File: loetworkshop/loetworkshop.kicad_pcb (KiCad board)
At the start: 2 copper layers, 50 x 100 mm, 14 parts, among them SW1 ON, SW2 OFF, SW3 SW_Push_SPDT, U1 CD40107BE, U2 NE555P

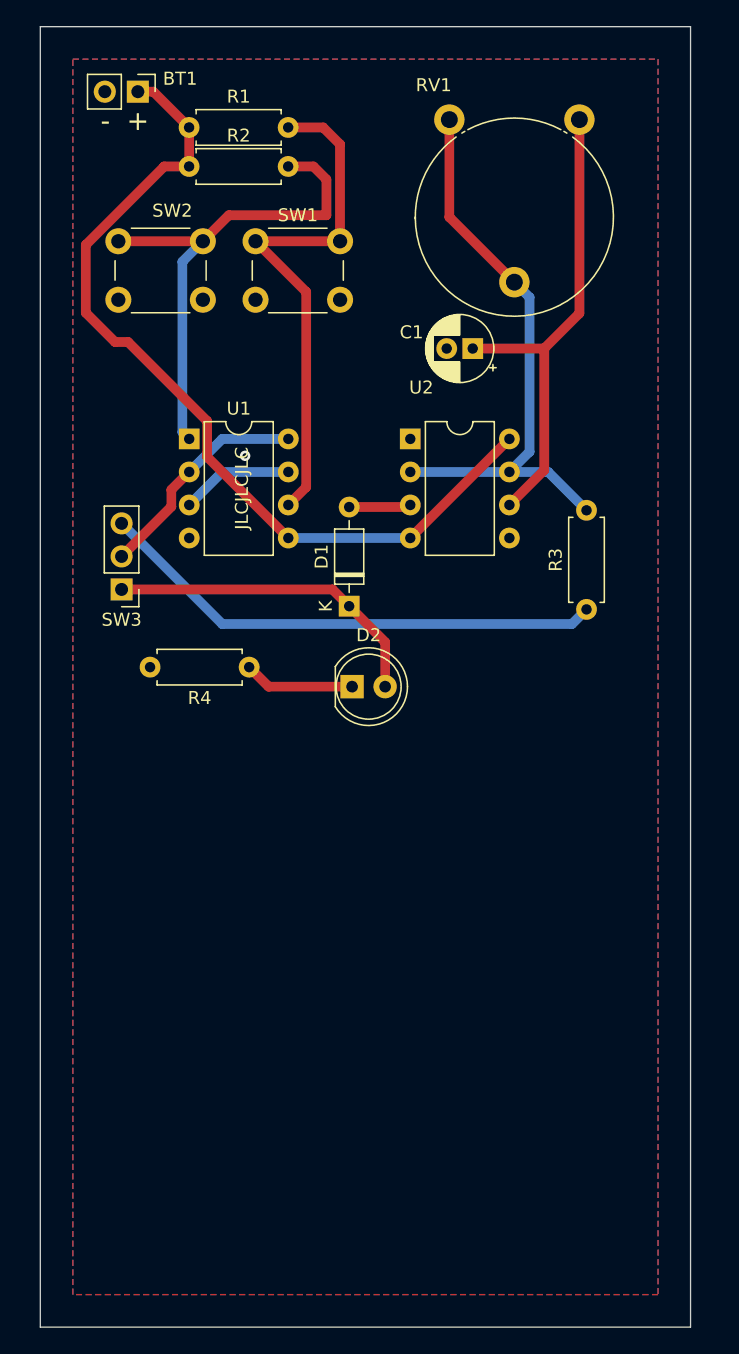
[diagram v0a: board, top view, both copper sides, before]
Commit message: added third soldering challenge
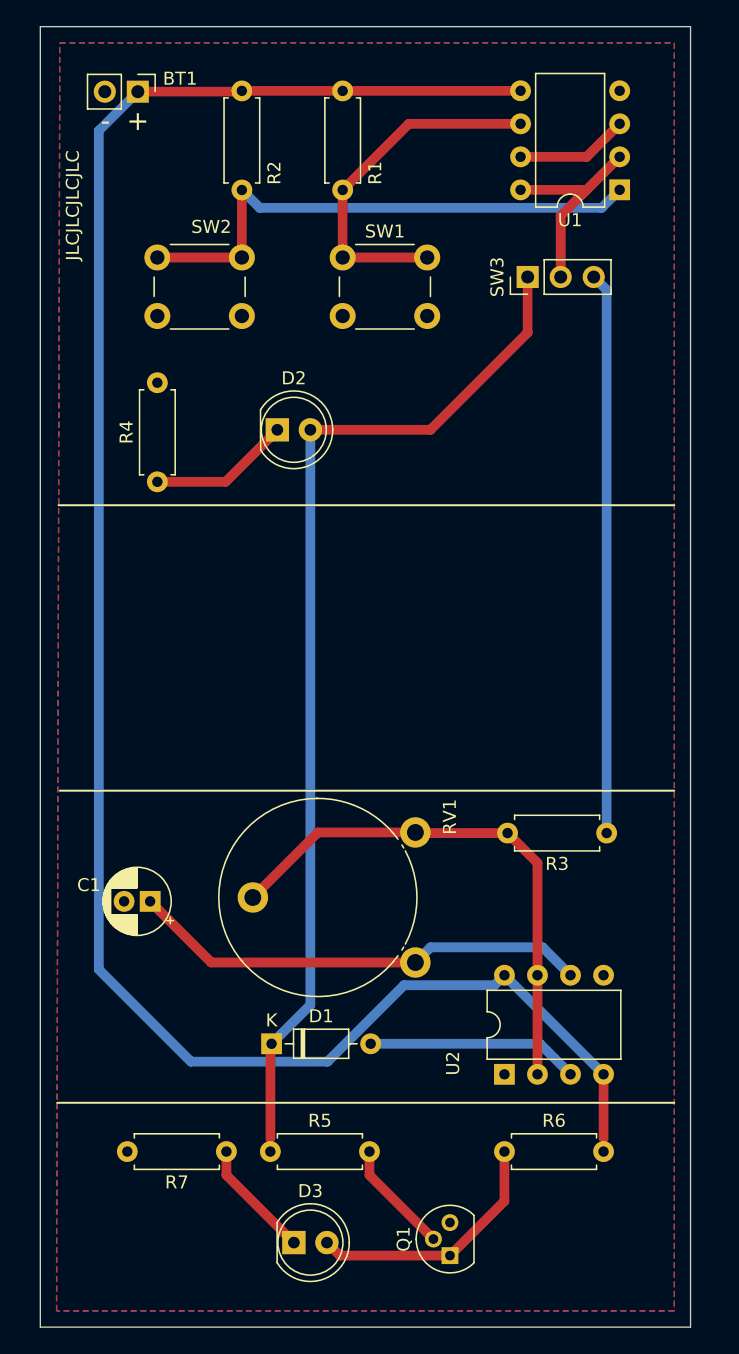
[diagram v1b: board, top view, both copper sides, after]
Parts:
- added D3: LED, LED_THT:LED_D5.0mm, F.Cu at (32.0, 106.0)
- added Q1: Q_NPN_CBE, Package_TO_SOT_THT:TO-92, F.Cu at (44.0, 107.0)
- added R5: 1K, Resistor_THT:R_Axial_DIN0207_L6.3mm_D2.5mm_P7.62mm_Horizontal, F.Cu at (30.2, 99.0)
- added R6: 1K, Resistor_THT:R_Axial_DIN0207_L6.3mm_D2.5mm_P7.62mm_Horizontal, F.Cu at (48.2, 99.0)
- added R7: 1K, Resistor_THT:R_Axial_DIN0207_L6.3mm_D2.5mm_P7.62mm_Horizontal, F.Cu at (26.8, 99.0)
- moved RV1 54.9 mm to (41.3, 74.5), turned to 180 degrees
- moved U2 49.4 mm to (48.2, 93.1), turned to 90 degrees
- moved C1 49.2 mm to (20.9, 79.8)
- moved SW3 39.4 mm to (50.0, 31.8), turned to 90 degrees
- moved U1 38.2 mm to (57.0, 25.1), turned to 180 degrees
- moved D1 34.2 mm to (30.3, 90.7), turned to 0 degrees
- moved D2 20.6 mm to (30.7, 43.5)
- moved R3 17.3 mm to (56.0, 74.5), turned to 180 degrees
- moved R4 15.9 mm to (21.5, 47.5), turned to 90 degrees
- moved R1 12.1 mm to (35.8, 17.4), turned to -90 degrees
- moved R2 7.09 mm to (28.0, 17.4), turned to -90 degrees
- moved SW1 6.82 mm to (35.8, 30.2)
- moved SW2 3.25 mm to (21.5, 30.2)
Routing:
- net +9V: track 68.3 -> 150.8 mm
- net /Drive_Constant: track 25.4 -> 79.9 mm
- net Net-(D3-Pad2): track 0.00 -> 19.6 mm
- net /On_Button: track 40.9 -> 27.5 mm
- net Net-(D1-Pad2): track 4.77 -> 16.3 mm
- net Net-(D3-Pad1): track 0.00 -> 9.15 mm
- net Net-(Q1-Pad2): track 0.00 -> 8.77 mm
- net /Discharge: track 45.1 -> 41.2 mm
- net /Drive_Timer: track 39.4 -> 43.2 mm
- net /Off_Button: track 39.0 -> 41.9 mm
- net Net-(D2-Pad1): track 8.54 -> 10.9 mm
- net /Threshold: track 37.4 -> 35.6 mm
- net Net-(SW3-Pad2): track 17.3 -> 16.2 mm
- net GND: vias 1 -> 0
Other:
- board text added: "JLCJLCJLCJLC"
- board text removed: "JLCJLCJLC"

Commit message: new pcb layout
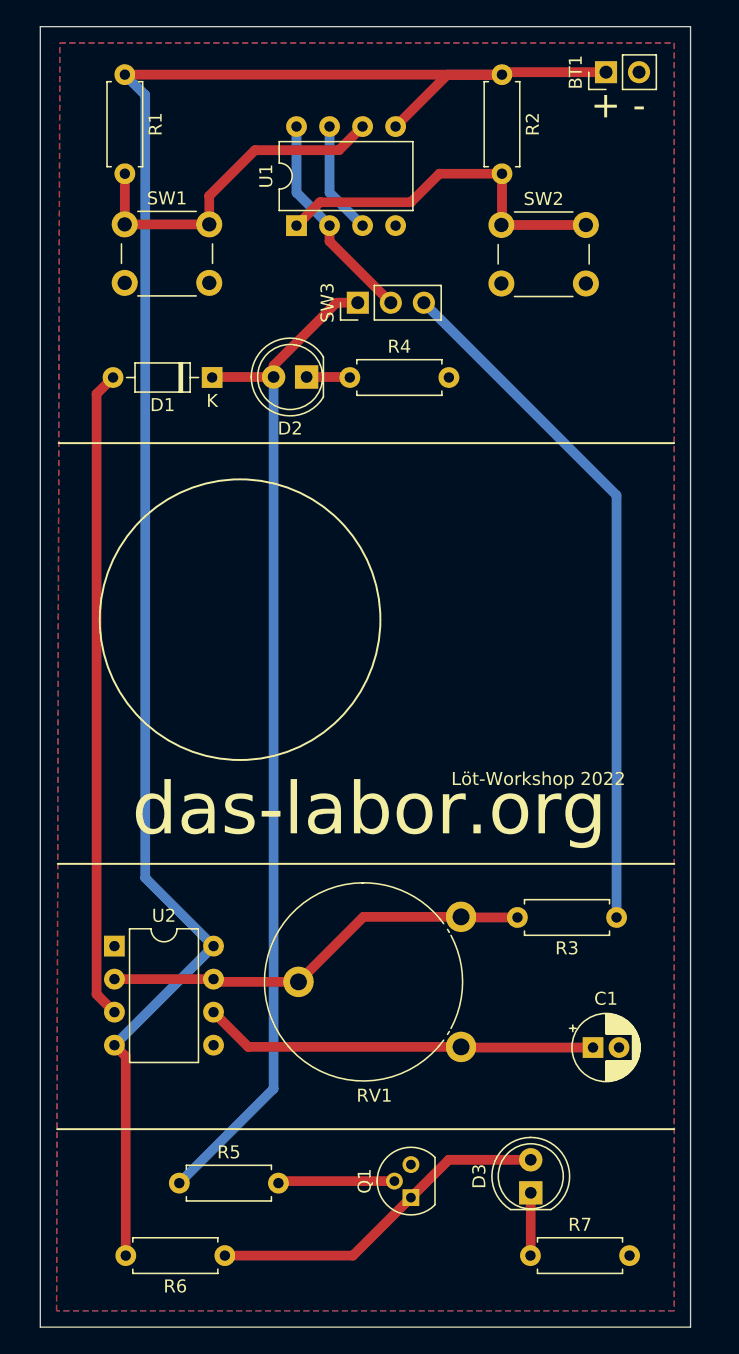
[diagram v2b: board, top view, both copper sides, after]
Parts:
- R1, R2: value 50K -> 10K
- R5: value 1K -> 10K
- moved D1 51.4 mm to (25.7, 39.5), turned to 180 degrees
- moved BT1 36.0 mm to (56.0, 16.0), turned to 90 degrees
- moved C1 35.9 mm to (55.0, 91.0), turned to 0 degrees
- moved U2 31.6 mm to (18.2, 83.2), turned to 0 degrees
- moved SW2 26.6 mm to (48.0, 27.8)
- moved U1 25.0 mm to (32.2, 27.8), turned to 90 degrees
- moved R7 24.7 mm to (50.2, 107.0), turned to 0 degrees
- moved R6 22.9 mm to (26.7, 107.0), turned to 180 degrees
- moved R2 20.0 mm to (48.0, 16.2)
- moved D3 18.6 mm to (50.2, 102.2), turned to 90 degrees
- moved SW1 17.0 mm to (19.0, 27.7)
- moved R4 16.8 mm to (36.3, 39.5), turned to 0 degrees
- moved R1 16.8 mm to (19.0, 16.2)
- moved SW3 13.2 mm to (36.9, 33.7)
- moved R5 7.41 mm to (23.2, 101.4)
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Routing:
- net Net-(D1-Pad2): track 16.3 -> 49.9 mm
- net /Off_Button: track 41.9 -> 28.1 mm
- net /Drive_Timer: track 43.2 -> 53.4 mm
- net /Discharge: track 41.2 -> 33.2 mm
- net Net-(D2-Pad1): track 10.9 -> 3.34 mm
- net Net-(D3-Pad2): track 19.6 -> 26.6 mm
- net +9V: track 150.8 -> 144.1 mm
- net /Threshold: track 35.6 -> 30.3 mm
- net Net-(D3-Pad1): track 9.15 -> 4.84 mm
- net /On_Button: track 27.5 -> 26.6 mm
- net /Drive_Constant: track 79.9 -> 79.1 mm
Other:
- board text added: "Created by: CodingChris - Kanga - Favo"
- board text added: "Löt-Workshop 2022"
- board text added: "das-labor.org"

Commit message: rev 1
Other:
- board text added: "Created by: CodingChris - Favo - Kanga"
- board text added: "Schnupperlöten"
- board text removed: "Created by: CodingChris - Kanga - Favo"
- board text removed: "Löt-Workshop 2022"
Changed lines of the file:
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@@
   (gr_line (start 12.5 12.5) (end 62.5 12.5) (layer "Edge.Cuts") (width 0.1))
   (gr_line (start 12.5 112.5) (end 12.5 12.5) (layer "Edge.Cuts") (width 0.1))
-  (gr_text "Created by:\nCodingChris - Kanga - Favo" (at 46.975 74.6) (layer "B.SilkS")
+  (gr_text "Created by:\nCodingChris - Favo - Kanga" (at 47.375 73.475) (layer "B.SilkS")
     (effects (font (size 1 1) (thickness 0.15)) (justify mirror))
   )
@@
     (effects (font (size 2 2) (thickness 0.3)))
   )
-  (gr_text "Löt-Workshop 2022" (at 50.8 70.35) (layer "F.SilkS")
+  (gr_text "Schnupperlöten\n" (at 52.8 70.375) (layer "F.SilkS")
     (effects (font (size 1 1) (thickness 0.15)))
   )

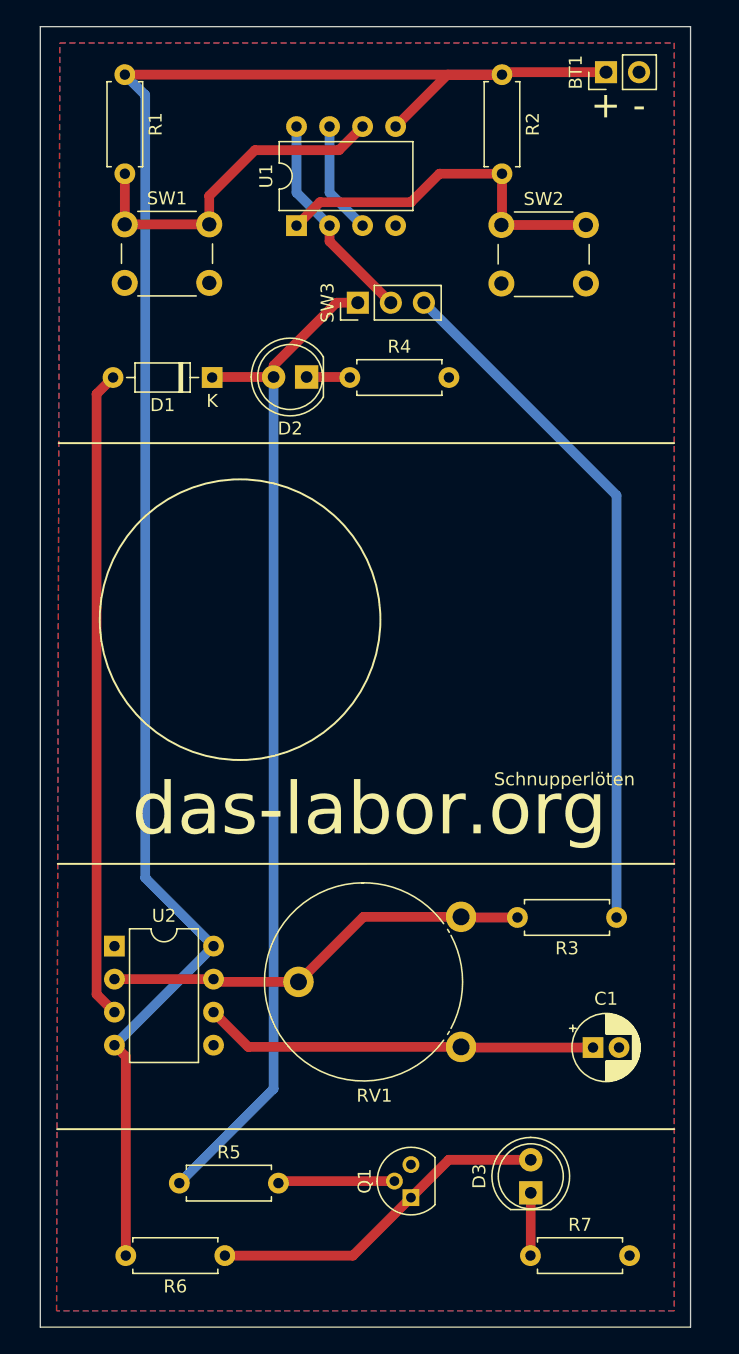
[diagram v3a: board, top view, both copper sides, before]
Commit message: rev 1.1 - fixed IC Pinout in the Footprint
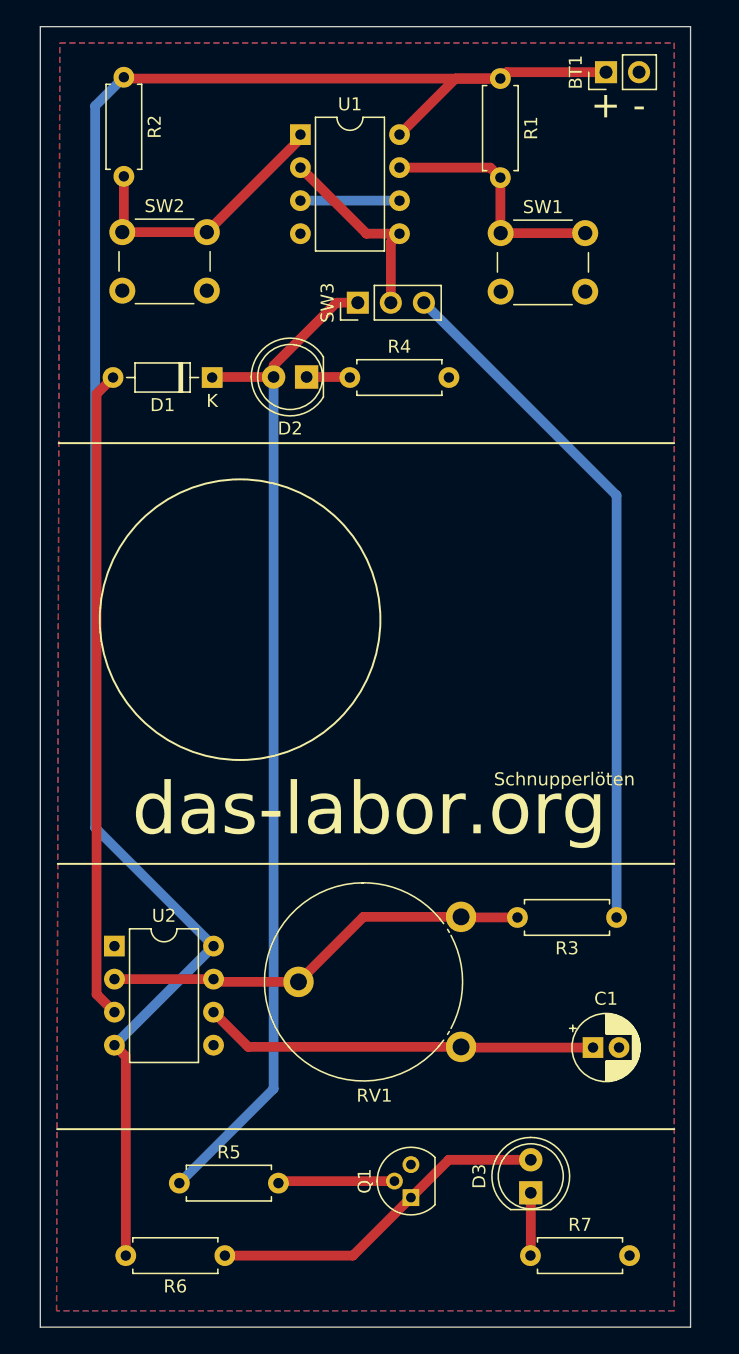
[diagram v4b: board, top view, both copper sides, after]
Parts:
- U1: footprint Package_DIP:DIP-8_W7.62mm -> switch_footprints:DIP-8_W7.62mm_InvertedDualRow
- moved SW2 29.2 mm to (18.8, 28.3)
- moved R2 29.1 mm to (18.9, 16.4)
- moved SW1 28.9 mm to (47.9, 28.4)
- moved R1 28.9 mm to (47.9, 16.5)
- moved U1 7.01 mm to (32.5, 20.8), turned to 0 degrees
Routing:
- net /On_Button: track 26.6 -> 18.8 mm
- net /Off_Button: track 28.1 -> 21.3 mm
- net +9V: track 144.1 -> 145.7 mm
- net Net-(SW3-Pad2): track 16.6 -> 15.3 mm
- net Net-(U1-Pad3): track 8.67 -> 7.62 mm

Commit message: rev 1.2
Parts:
- U1: footprint switch_footprints:DIP-8_W7.62mm_InvertedDualRow -> Package_DIP:DIP-8_W7.62mm
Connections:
- U1 pad 5: +9V -> Net-(SW3-Pad2)
- U1 pad 6: /On_Button -> Net-(U1-Pad3)
- U1 pad 7: Net-(U1-Pad3) -> /On_Button
- U1 pad 8: Net-(SW3-Pad2) -> +9V
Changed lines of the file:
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@@
     )
   )
-  (footprint "switch_footprints:DIP-8_W7.62mm_InvertedDualRow" (layer "F.Cu")
+  (footprint "Package_DIP:DIP-8_W7.62mm" (layer "F.Cu")
     (at 32.5 20.8)
     (descr "8-lead though-hole mounted DIP package, row spacing 7.62 mm (300 mils)")
@@
     )
     (fp_line (start 6.46 8.95) (end 6.46 -1.33) (layer "F.SilkS") (width 0.12))
+    (fp_line (start 6.46 -1.33) (end 4.81 -1.33) (layer "F.SilkS") (width 0.12))
     (fp_line (start 2.81 -1.33) (end 1.16 -1.33) (layer "F.SilkS") (width 0.12))
+    (fp_line (start 1.16 8.95) (end 6.46 8.95) (layer "F.SilkS") (width 0.12))
     (fp_line (start 1.16 -1.33) (end 1.16 8.95) (layer "F.SilkS") (width 0.12))
-    (fp_line (start 6.46 -1.33) (end 4.81 -1.33) (layer "F.SilkS") (width 0.12))
-    (fp_line (start 1.16 8.95) (end 6.46 8.95) (layer "F.SilkS") (width 0.12))
     (fp_arc (start 4.81 -1.33) (mid 3.81 -0.33) (end 2.81 -1.33) (layer "F.SilkS") (width 0.12))
     (fp_line (start -1.1 9.15) (end 8.7 9.15) (layer "F.CrtYd") (width 0.05))
+    (fp_line (start 8.7 9.15) (end 8.7 -1.55) (layer "F.CrtYd") (width 0.05))
+    (fp_line (start -1.1 -1.55) (end -1.1 9.15) (layer "F.CrtYd") (width 0.05))
     (fp_line (start 8.7 -1.55) (end -1.1 -1.55) (layer "F.CrtYd") (width 0.05))
-    (fp_line (start -1.1 -1.55) (end -1.1 9.15) (layer "F.CrtYd") (width 0.05))
-    (fp_line (start 8.7 9.15) (end 8.7 -1.55) (layer "F.CrtYd") (width 0.05))
+    (fp_line (start 6.985 8.89) (end 0.635 8.89) (layer "F.Fab") (width 0.1))
+    (fp_line (start 0.635 -0.27) (end 1.635 -1.27) (layer "F.Fab") (width 0.1))
+    (fp_line (start 1.635 -1.27) (end 6.985 -1.27) (layer "F.Fab") (width 0.1))
     (fp_line (start 0.635 8.89) (end 0.635 -0.27) (layer "F.Fab") (width 0.1))
     (fp_line (start 6.985 -1.27) (end 6.985 8.89) (layer "F.Fab") (width 0.1))
-    (fp_line (start 1.635 -1.27) (end 6.985 -1.27) (layer "F.Fab") (width 0.1))
-    (fp_line (start 6.985 8.89) (end 0.635 8.89) (layer "F.Fab") (width 0.1))
-    (fp_line (start 0.635 -0.27) (end 1.635 -1.27) (layer "F.Fab") (width 0.1))
-    (pad "1" thru_hole rect (at 0 0) (size 1.6 1.6) (drill 0.8) (layers *.Cu *.Mask)
+    (pad "1" thru_hole rect locked (at 0 0) (size 1.6 1.6) (drill 0.8) (layers *.Cu *.Mask)
       (net 11 "/Off_Button") (pinfunction "A") (pintype "input"))
-    (pad "2" thru_hole oval (at 0 2.54) (size 1.6 1.6) (drill 0.8) (layers *.Cu *.Mask)
+    (pad "2" thru_hole oval locked (at 0 2.54) (size 1.6 1.6) (drill 0.8) (layers *.Cu *.Mask)
       (net 14 "Net-(SW3-Pad2)") (pinfunction "B") (pintype "input"))
-    (pad "3" thru_hole oval (at 0 5.08) (size 1.6 1.6) (drill 0.8) (layers *.Cu *.Mask)
+    (pad "3" thru_hole oval locked (at 0 5.08) (size 1.6 1.6) (drill 0.8) (layers *.Cu *.Mask)
       (net 15 "Net-(U1-Pad3)") (pinfunction "C") (pintype "output"))
-    (pad "4" thru_hole oval (at 0 7.62) (size 1.6 1.6) (drill 0.8) (layers *.Cu *.Mask)
+    (pad "4" thru_hole oval locked (at 0 7.62) (size 1.6 1.6) (drill 0.8) (layers *.Cu *.Mask)
       (net 1 "GND") (pinfunction "GND") (pintype "power_in"))
-    (pad "5" thru_hole oval (at 7.62 0) (size 1.6 1.6) (drill 0.8) (layers *.Cu *.Mask)
+    (pad "5" thru_hole oval locked (at 7.62 7.62) (size 1.6 1.6) (drill 0.8) (layers *.Cu *.Mask)
+      (net 14 "Net-(SW3-Pad2)") (pinfunction "F") (pintype "output"))
+    (pad "6" thru_hole oval locked (at 7.62 5.08) (size 1.6 1.6) (drill 0.8) (layers *.Cu *.Mask)
+      (net 15 "Net-(U1-Pad3)") (pinfunction "E") (pintype "input"))
+    (pad "7" thru_hole oval locked (at 7.62 2.54) (size 1.6 1.6) (drill 0.8) (layers *.Cu *.Mask)
+      (net 10 "/On_Button") (pinfunction "D") (pintype "input"))
+    (pad "8" thru_hole oval locked (at 7.62 0) (size 1.6 1.6) (drill 0.8) (layers *.Cu *.Mask)
       (net 2 "+9V") (pinfunction "VCC") (pintype "power_in"))
-    (pad "6" thru_hole oval (at 7.62 2.54) (size 1.6 1.6) (drill 0.8) (layers *.Cu *.Mask)
-      (net 10 "/On_Button") (pinfunction "D") (pintype "input"))
-    (pad "7" thru_hole oval (at 7.62 5.08) (size 1.6 1.6) (drill 0.8) (layers *.Cu *.Mask)
-      (net 15 "Net-(U1-Pad3)") (pinfunction "E") (pintype "input"))
-    (pad "8" thru_hole oval (at 7.62 7.62) (size 1.6 1.6) (drill 0.8) (layers *.Cu *.Mask)
-      (net 14 "Net-(SW3-Pad2)") (pinfunction "F") (pintype "output"))
     (model "${KICAD6_3DMODEL_DIR}/Package_DIP.3dshapes/DIP-8_W7.62mm.wrl"
       (offset (xyz 0 0 0))
@@
     (fp_line (start 1.921 1.04) (end 1.921 2.414) (layer "F.SilkS") (width 0.12))
     (fp_line (start 1 1.04) (end 1 2.58) (layer "F.SilkS") (width 0.12))
+    (fp_line (start 3.121 -1.5) (end 3.121 1.5) (layer "F.SilkS") (width 0.12))
     (fp_line (start 2.241 1.04) (end 2.241 2.268) (layer "F.SilkS") (width 0.12))
-    (fp_line (start 3.161 -1.443) (end 3.161 1.443) (layer "F.SilkS") (width 0.12))
     (fp_line (start 1.12 -2.578) (end 1.12 -1.04) (layer "F.SilkS") (width 0.12))
     (fp_line (start 3.321 -1.178) (end 3.321 1.178) (layer "F.SilkS") (width 0.12))
@@
     (fp_line (start 3.561 -0.518) (end 3.561 0.518) (layer "F.SilkS") (width 0.12))
     (fp_line (start 2.641 -2.004) (end 2.641 -1.04) (layer "F.SilkS") (width 0.12))
+    (fp_line (start 3.161 -1.443) (end 3.161 1.443) (layer "F.SilkS") (width 0.12))
     (fp_line (start 2.361 1.04) (end 2.361 2.2) (layer "F.SilkS") (width 0.12))
     (fp_line (start 3.001 -1.653) (end 3.001 -1.04) (layer "F.SilkS") (width 0.12))
@@
     (fp_line (start 1.56 1.04) (end 1.56 2.52) (layer "F.SilkS") (width 0.12))
     (fp_line (start 1.48 -2.536) (end 1.48 -1.04) (layer "F.SilkS") (width 0.12))
-    (fp_line (start 3.121 -1.5) (end 3.121 1.5) (layer "F.SilkS") (width 0.12))
     (fp_circle (center 1 0) (end 3.62 0) (layer "F.SilkS") (width 0.12) (fill none))
     (fp_circle (center 1 0) (end 3.75 0) (layer "F.CrtYd") (width 0.05) (fill none))

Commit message: rev 1.3 - more footprint fixes
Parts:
- U2: footprint Package_DIP:DIP-8_W7.62mm -> switch_footprints:DIP-8_W7.62mm_InvertedDualRow
- moved R3 41.5 mm to (15.3, 80.4), turned to 0 degrees
- moved C1 35.1 mm to (20.0, 91.8), turned to 180 degrees
- moved U2 33.8 mm to (52.0, 84.2), turned to -90 degrees
- moved R5 30.3 mm to (53.3, 104.7), turned to 180 degrees
- moved R7 27.2 mm to (23.2, 103.5), turned to 180 degrees
- moved D1 25.8 mm to (51.3, 36.6), turned to -90 degrees
- moved D3 21.5 mm to (28.7, 103.3), turned to 0 degrees
- moved R6 19.9 mm to (45.6, 101.0), turned to 0 degrees
- moved D2 8.41 mm to (41.4, 39.8), turned to 0 degrees
- moved RV1 5.27 mm to (39.6, 80.5)
- moved SW3 5.06 mm to (42.0, 33.6), turned to -90 degrees
- moved Q1 3.75 mm to (37.4, 103.4), turned to -90 degrees
- moved R4 0.43 mm to (36.6, 39.8), turned to 180 degrees
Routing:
- net +9V: track 145.7 -> 133.3 mm
- net Net-(D3-Pad2): track 26.6 -> 15.4 mm
- net /Discharge: track 33.2 -> 43.6 mm
- net Net-(D1-Pad2): track 49.9 -> 41.8 mm
- net /Drive_Constant: track 79.1 -> 86.7 mm
- net /Drive_Timer: track 53.4 -> 57.9 mm
- net Net-(Q1-Pad2): track 8.99 -> 7.04 mm
- net Net-(D2-Pad1): track 3.34 -> 4.79 mm
- net /Threshold: track 30.3 -> 31.6 mm
- net Net-(D3-Pad1): track 4.84 -> 5.59 mm
- net GND: vias 0 -> 16
